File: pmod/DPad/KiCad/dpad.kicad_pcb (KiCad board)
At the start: 2 copper layers, 49 x 36 mm, 13 parts, among them SW1 SW_Push, SW2 SW_Push, SW3 SW_Push, SW4 SW_Push

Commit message: Fixed resistor labels to correct format (10K).
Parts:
- R1, R2, R3, R4: value 10 k -> 10K
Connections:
- net io1 renamed IO1
- net io2 renamed IO2
- net io3 renamed IO3
- net io4 renamed IO4
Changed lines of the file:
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@@
 	)
 	(net 0 "")
-	(net 1 "io3")
-	(net 2 "io4")
-	(net 3 "io2")
-	(net 4 "io1")
+	(net 1 "IO3")
+	(net 2 "IO4")
+	(net 3 "IO2")
+	(net 4 "IO1")
 	(net 5 "/GND")
 	(net 6 "/VCC")
@@
 			)
 		)
-		(property "Value" "10 k"
+		(property "Value" "10K"
 			(at 2.54 0 0)
 			(layer "F.Fab")
@@
 			(layers "*.Cu" "*.Mask")
 			(remove_unused_layers no)
-			(net 4 "io1")
+			(net 4 "IO1")
 			(pintype "passive")
 		)
@@
 			(layers "*.Cu" "*.Mask")
 			(remove_unused_layers no)
-			(net 4 "io1")
+			(net 4 "IO1")
 			(pinfunction "IO1")
 			(pintype "passive")
@@
 			(layers "*.Cu" "*.Mask")
 			(remove_unused_layers no)
-			(net 3 "io2")
+			(net 3 "IO2")
 			(pinfunction "IO2")
 			(pintype "passive")
@@
 			(layers "*.Cu" "*.Mask")
 			(remove_unused_layers no)
-			(net 1 "io3")
+			(net 1 "IO3")
 			(pinfunction "IO3")
 			(pintype "passive")
@@
 			(layers "*.Cu" "*.Mask")
 			(remove_unused_layers no)
-			(net 2 "io4")
+			(net 2 "IO4")
 			(pinfunction "IO4")
 			(pintype "passive")
@@
 			(layers "*.Cu" "*.Mask")
 			(remove_unused_layers no)
-			(net 4 "io1")
+			(net 4 "IO1")
 			(pinfunction "1")
 			(pintype "passive")
@@
 			(layers "*.Cu" "*.Mask")
 			(remove_unused_layers no)
-			(net 4 "io1")
+			(net 4 "IO1")
 			(pinfunction "1")
 			(pintype "passive")
@@
 			)
 		)
-		(property "Value" "10 k"
+		(property "Value" "10K"
 			(at 2.54 0 0)
 			(layer "F.Fab")
@@
 			(layers "*.Cu" "*.Mask")
 			(remove_unused_layers no)
-			(net 2 "io4")
+			(net 2 "IO4")
 			(pintype "passive")
 		)
@@
 			(layers "*.Cu" "*.Mask")
 			(remove_unused_layers no)
-			(net 1 "io3")
+			(net 1 "IO3")
 			(pinfunction "1")
 			(pintype "passive")
@@
 			(layers "*.Cu" "*.Mask")
 			(remove_unused_layers no)
-			(net 1 "io3")
+			(net 1 "IO3")
 			(pinfunction "1")
 			(pintype "passive")
@@
 			)
 		)
-		(property "Value" "10 k"
+		(property "Value" "10K"
 			(at 2.54 0 90)
 			(layer "F.Fab")
@@
 			(layers "*.Cu" "*.Mask")
 			(remove_unused_layers no)
-			(net 3 "io2")
+			(net 3 "IO2")
 			(pintype "passive")
 		)
@@
 			)
 		)
-		(property "Value" "10 k"
+		(property "Value" "10K"
 			(at 2.54 0 0)
 			(layer "F.Fab")
@@
 			(layers "*.Cu" "*.Mask")
 			(remove_unused_layers no)
-			(net 1 "io3")
+			(net 1 "IO3")
 			(pintype "passive")
 		)
@@
 			(layers "*.Cu" "*.Mask")
 			(remove_unused_layers no)
-			(net 2 "io4")
+			(net 2 "IO4")
 			(pinfunction "1")
 			(pintype "passive")
@@
 			(layers "*.Cu" "*.Mask")
 			(remove_unused_layers no)
-			(net 2 "io4")
+			(net 2 "IO4")
 			(pinfunction "1")
 			(pintype "passive")
@@
 			(layers "*.Cu" "*.Mask")
 			(remove_unused_layers no)
-			(net 3 "io2")
+			(net 3 "IO2")
 			(pinfunction "1")
 			(pintype "passive")
@@
 			(layers "*.Cu" "*.Mask")
 			(remove_unused_layers no)
-			(net 3 "io2")
+			(net 3 "IO2")
 			(pinfunction "1")
 			(pintype "passive")

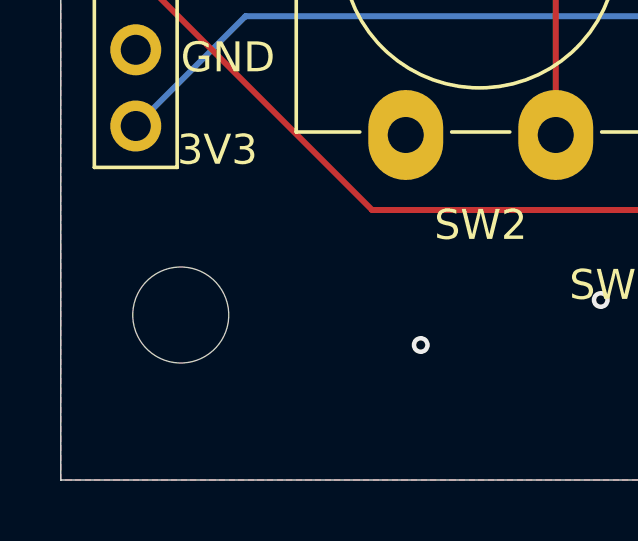
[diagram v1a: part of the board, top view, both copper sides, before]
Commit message: Fixed left bottom hole position to be correctly aligned
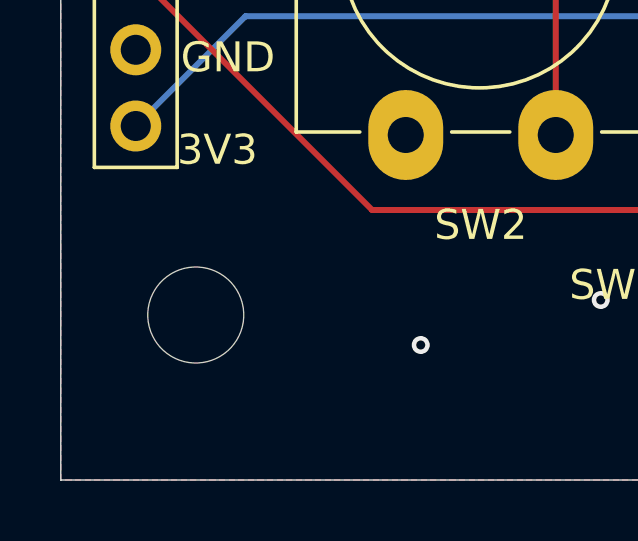
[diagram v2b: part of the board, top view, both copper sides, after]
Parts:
- moved H4 0.50 mm to (93.0, 117.5)
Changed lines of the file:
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@@
 	(footprint "MountingHole:MountingHole_3.2mm_M3"
 		(layer "F.Cu")
-		(at 92.5 117.5)
+		(at 93 117.5)
 		(descr "Mounting Hole 3.2mm, M3, no annular, generated by kicad-footprint-generator mountinghole.py")
 		(tags "mountinghole M3")

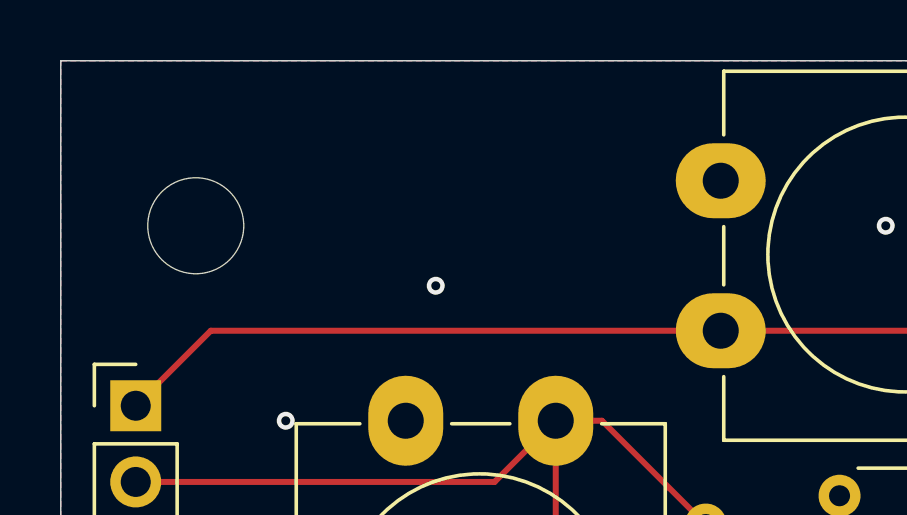
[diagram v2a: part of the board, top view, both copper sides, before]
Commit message: Added labels and logo to board silkscreen
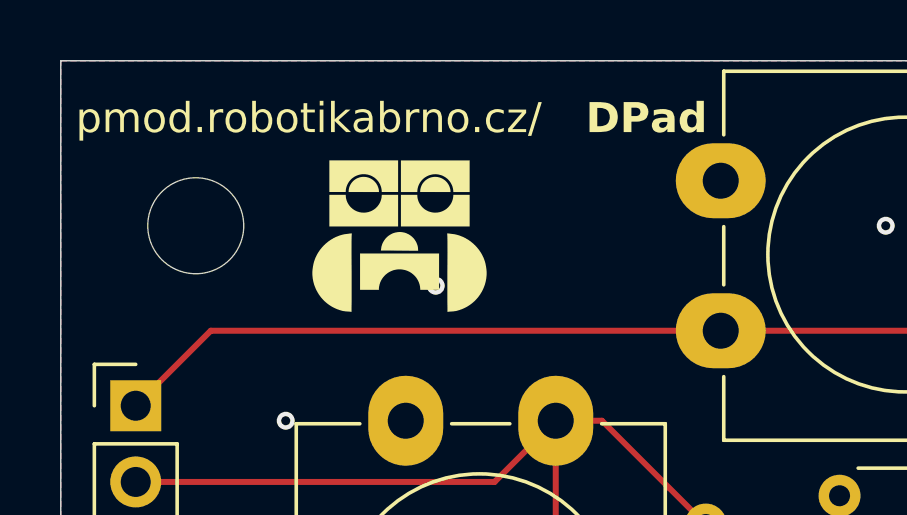
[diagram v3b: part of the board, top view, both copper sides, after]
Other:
- board text added: "DPad"
- board text added: "pmod.robotikabrno.cz/"

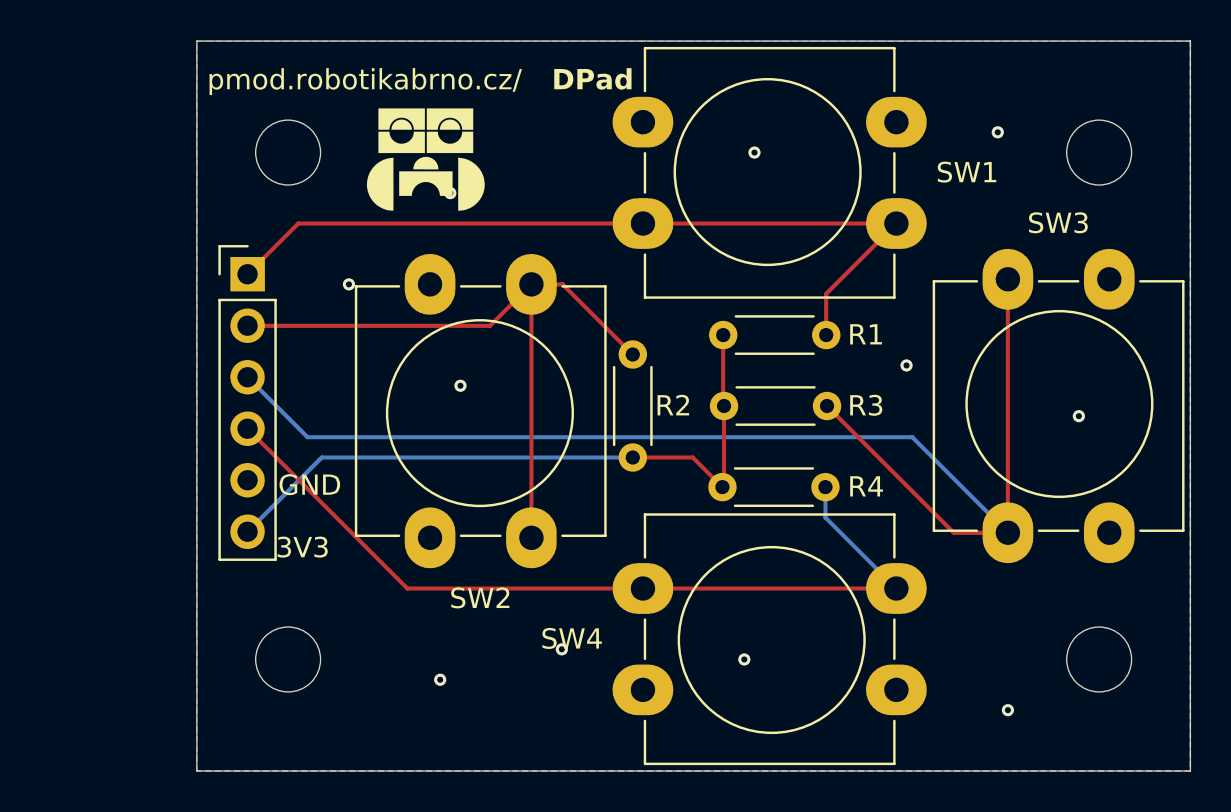
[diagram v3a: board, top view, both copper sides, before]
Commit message: Moved silkscreen labels, added dimension labels, added hole size labels
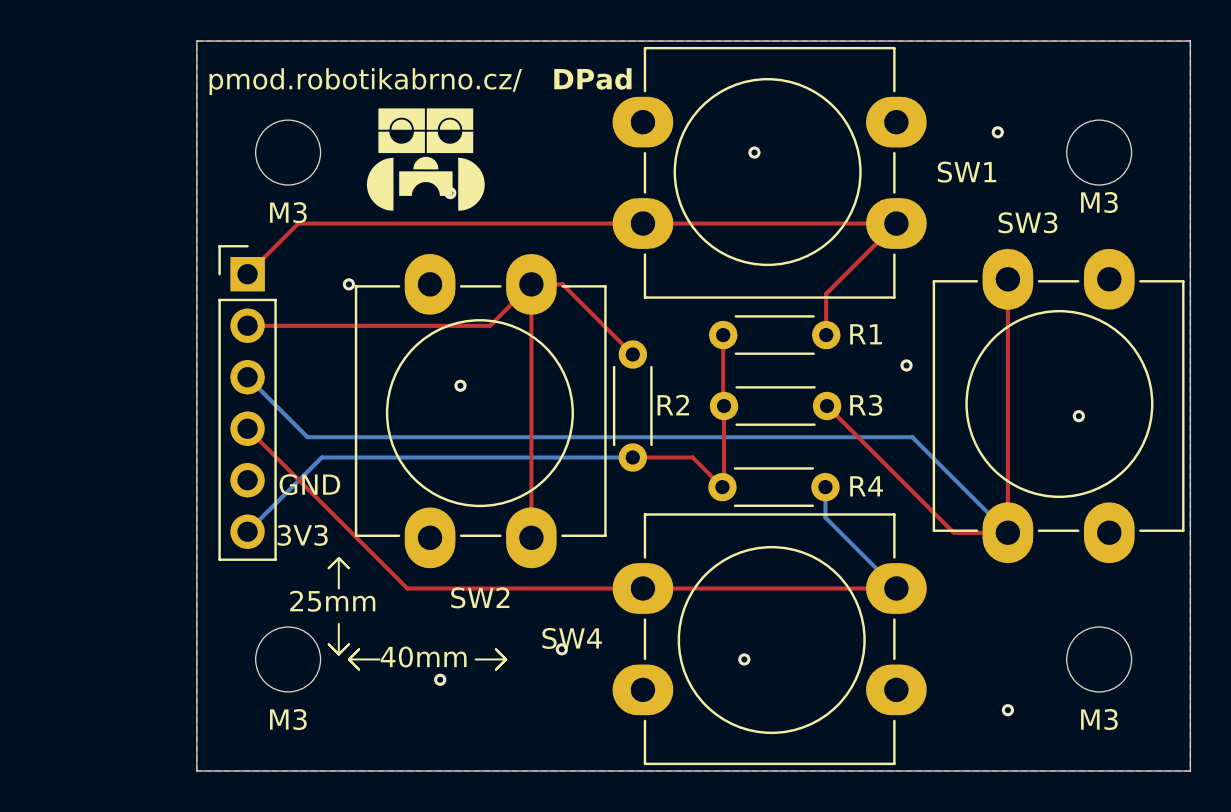
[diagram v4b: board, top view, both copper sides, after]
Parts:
- removed H1, H2, H3, H4: MountingHole, MountingHole:MountingHole_3.2mm_M3
- added M3: MountingHole_3.2mm_M3, MountingHole:MountingHole_3.2mm_M3, F.Cu at (93.0, 117.5)
- added M3: MountingHole_3.2mm_M3, MountingHole:MountingHole_3.2mm_M3, F.Cu at (133.0, 92.5)
- added M3: MountingHole_3.2mm_M3, MountingHole:MountingHole_3.2mm_M3, F.Cu at (93.0, 92.5)
- added M3: MountingHole_3.2mm_M3, MountingHole:MountingHole_3.2mm_M3, F.Cu at (133.0, 117.5)
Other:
- board text added: "25mm"
- board text added: "40mm"

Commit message: fix: small pcb fixes
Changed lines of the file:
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@@
 		(tags "mountinghole M3")
 		(property "Reference" "M3"
-			(at 0 2.5 0)
+			(at 0 3.004 0)
 			(layer "F.SilkS")
 			(effects
@@
 		(start 119.58 105)
 		(end 125.83 111.25)
-		(width 0.2)
+		(width 0.3)
 		(layer "F.Cu")
 		(net 1)
@@
 		(start 125.83 111.25)
 		(end 128.5 111.25)
-		(width 0.2)
+		(width 0.3)
 		(layer "F.Cu")
 		(net 1)
@@
 		(start 128.5 111.25)
 		(end 128.5 98.75)
-		(width 0.2)
+		(width 0.3)
 		(layer "F.Cu")
 		(net 1)
 	)
 	(segment
-		(start 128.5 111.25)
-		(end 123.789 106.539)
-		(width 0.2)
+		(start 112.268 106.172)
+		(end 93.592 106.172)
+		(width 0.3)
 		(layer "B.Cu")
 		(net 1)
 	)
 	(segment
-		(start 123.789 106.539)
-		(end 93.959 106.539)
-		(width 0.2)
+		(start 93.592 106.172)
+		(end 91 103.58)
+		(width 0.3)
 		(layer "B.Cu")
 		(net 1)
 	)
 	(segment
-		(start 93.959 106.539)
-		(end 91 103.58)
-		(width 0.2)
+		(start 112.903 106.807)
+		(end 112.268 106.172)
+		(width 0.3)
+		(layer "B.Cu")
+		(net 1)
+	)
+	(segment
+		(start 124.057 106.807)
+		(end 112.903 106.807)
+		(width 0.3)
+		(layer "B.Cu")
+		(net 1)
+	)
+	(segment
+		(start 128.5 111.25)
+		(end 124.057 106.807)
+		(width 0.3)
 		(layer "B.Cu")
 		(net 1)
@@
 		(start 98.88 114)
 		(end 91 106.12)
-		(width 0.2)
+		(width 0.3)
 		(layer "F.Cu")
 		(net 2)
@@
 		(start 110.5 114)
 		(end 123 114)
-		(width 0.2)
+		(width 0.3)
 		(layer "F.Cu")
 		(net 2)
@@
 		(start 110.5 114)
 		(end 98.88 114)
-		(width 0.2)
+		(width 0.3)
 		(layer "F.Cu")
 		(net 2)
@@
 		(start 119.5 109)
 		(end 119.5 110.5)
-		(width 0.2)
+		(width 0.3)
 		(layer "B.Cu")
 		(net 2)
@@
 		(start 119.5 110.5)
 		(end 123 114)
-		(width 0.2)
+		(width 0.3)
 		(layer "B.Cu")
 		(net 2)
 	)
 	(segment
+		(start 102.527 101.473)
+		(end 91.433 101.473)
+		(width 0.3)
+		(layer "F.Cu")
+		(net 3)
+	)
+	(segment
 		(start 106.54 99)
 		(end 110 102.46)
-		(width 0.2)
+		(width 0.3)
 		(layer "F.Cu")
 		(net 3)
@@
 	(segment
 		(start 105 99)
-		(end 102.96 101.04)
-		(width 0.2)
+		(end 106.54 99)
+		(width 0.3)
 		(layer "F.Cu")
 		(net 3)
 	)
 	(segment
-		(start 105 99)
-		(end 106.54 99)
+		(start 91.433 101.473)
+		(end 91 101.04)
 		(width 0.2)
 		(layer "F.Cu")
@@
 	(segment
 		(start 105 99)
-		(end 105 111.5)
-		(width 0.2)
+		(end 102.527 101.473)
+		(width 0.3)
 		(layer "F.Cu")
 		(net 3)
 	)
 	(segment
-		(start 102.96 101.04)
-		(end 91 101.04)
-		(width 0.2)
+		(start 105 99)
+		(end 105 111.5)
+		(width 0.3)
 		(layer "F.Cu")
 		(net 3)
@@
 		(start 91 98.5)
 		(end 93.5 96)
-		(width 0.2)
+		(width 0.3)
 		(layer "F.Cu")
 		(net 4)
@@
 		(start 93.5 96)
 		(end 110.5 96)
-		(width 0.2)
+		(width 0.3)
 		(layer "F.Cu")
 		(net 4)
@@
 		(start 119.54 101.5)
 		(end 119.54 99.46)
-		(width 0.2)
+		(width 0.3)
 		(layer "F.Cu")
 		(net 4)
@@
 		(start 123 96)
 		(end 110.5 96)
-		(width 0.2)
+		(width 0.3)
 		(layer "F.Cu")
 		(net 4)
@@
 		(start 119.54 99.46)
 		(end 123 96)
-		(width 0.2)
+		(width 0.3)
 		(layer "F.Cu")
 		(net 4)
@@
 		(start 114.5 105)
 		(end 114.5 108.92)
-		(width 0.2)
+		(width 0.3)
 		(layer "F.Cu")
 		(net 6)
@@
 		(start 112.96 107.54)
 		(end 110 107.54)
-		(width 0.2)
+		(width 0.3)
 		(layer "F.Cu")
 		(net 6)
@@
 		(start 114.42 109)
 		(end 112.96 107.54)
-		(width 0.2)
+		(width 0.3)
 		(layer "F.Cu")
 		(net 6)
@@
 		(start 114.46 104.46)
 		(end 114.46 101.5)
-		(width 0.2)
+		(width 0.3)
 		(layer "F.Cu")
 		(net 6)
@@
 		(start 94.66 107.54)
 		(end 110 107.54)
-		(width 0.2)
+		(width 0.3)
 		(layer "B.Cu")
 		(net 6)

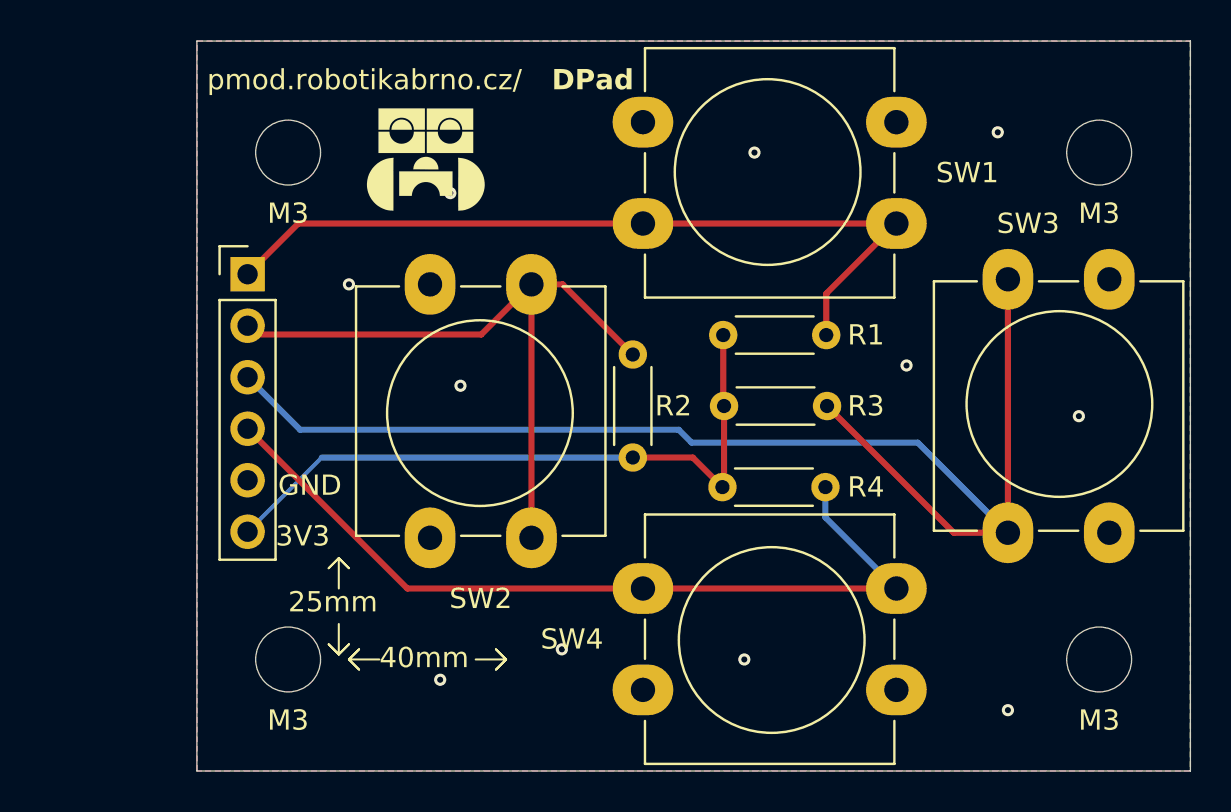
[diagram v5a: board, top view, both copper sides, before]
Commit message: Added debounce capacitors. Added drill holes for switches.
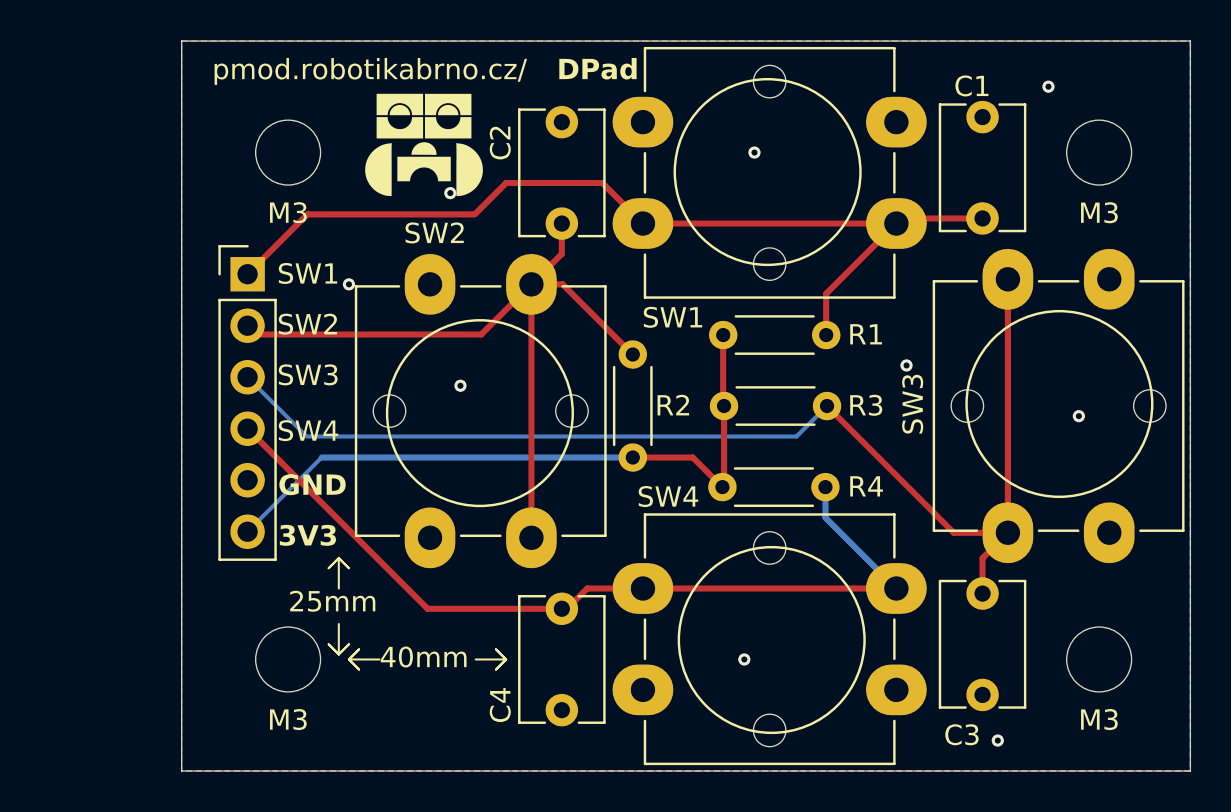
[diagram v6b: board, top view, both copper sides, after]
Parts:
- added C1: 1uF, Custom:C_Disc_D6.0mm_W4mm_P5.00mm, F.Cu at (127.2, 90.8)
- added C2: 1uF, Custom:C_Disc_D6.0mm_W4mm_P5.00mm, F.Cu at (106.5, 91.0)
- added C3: 1uF, Custom:C_Disc_D6.0mm_W4mm_P5.00mm, F.Cu at (127.2, 119.2)
- added C4: 1uF, Custom:C_Disc_D6.0mm_W4mm_P5.00mm, F.Cu at (106.5, 120.0)
- SW1, SW2, SW3, SW4: footprint Button_Switch_THT:SW_PUSH-12mm_Wuerth-430476085716 -> Custom:SW_PUSH-12mm
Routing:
- net IO3: track 64.7 -> 57.9 mm
- net IO1: track 40.0 -> 46.0 mm
- net IO2: track 34.1 -> 37.8 mm
- net IO4: track 41.7 -> 42.5 mm
- net /GND: vias 11 -> 9
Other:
- board size 49 x 36 mm -> 49.8 x 36 mm
- board text added: "SW2"
- board text added: "SW3"
- board text added: "SW4"

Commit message: Increased track width. Rounded edges of board. Fixed right angle connector.
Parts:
- PMOD1: footprint Connector_PinHeader_2.54mm:PinHeader_1x06_P2.54mm_Vertical -> Connector_PinHeader_2.54mm:PinHeader_1x06_P2.54mm_Horizontal
- moved PMOD1 8.77 mm to (82.2, 98.5)
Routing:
- net IO3: track 57.9 -> 57.3 mm
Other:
- board size 49.8 x 36 mm -> 50.8 x 36 mm
